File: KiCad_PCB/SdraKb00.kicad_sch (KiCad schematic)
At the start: 20 parts, among them J1 USB_C_Receptacle_USB2.0_16P, SW1 Reset_SW, U1 ATMEGA32U4-AU, Y1 16MHz

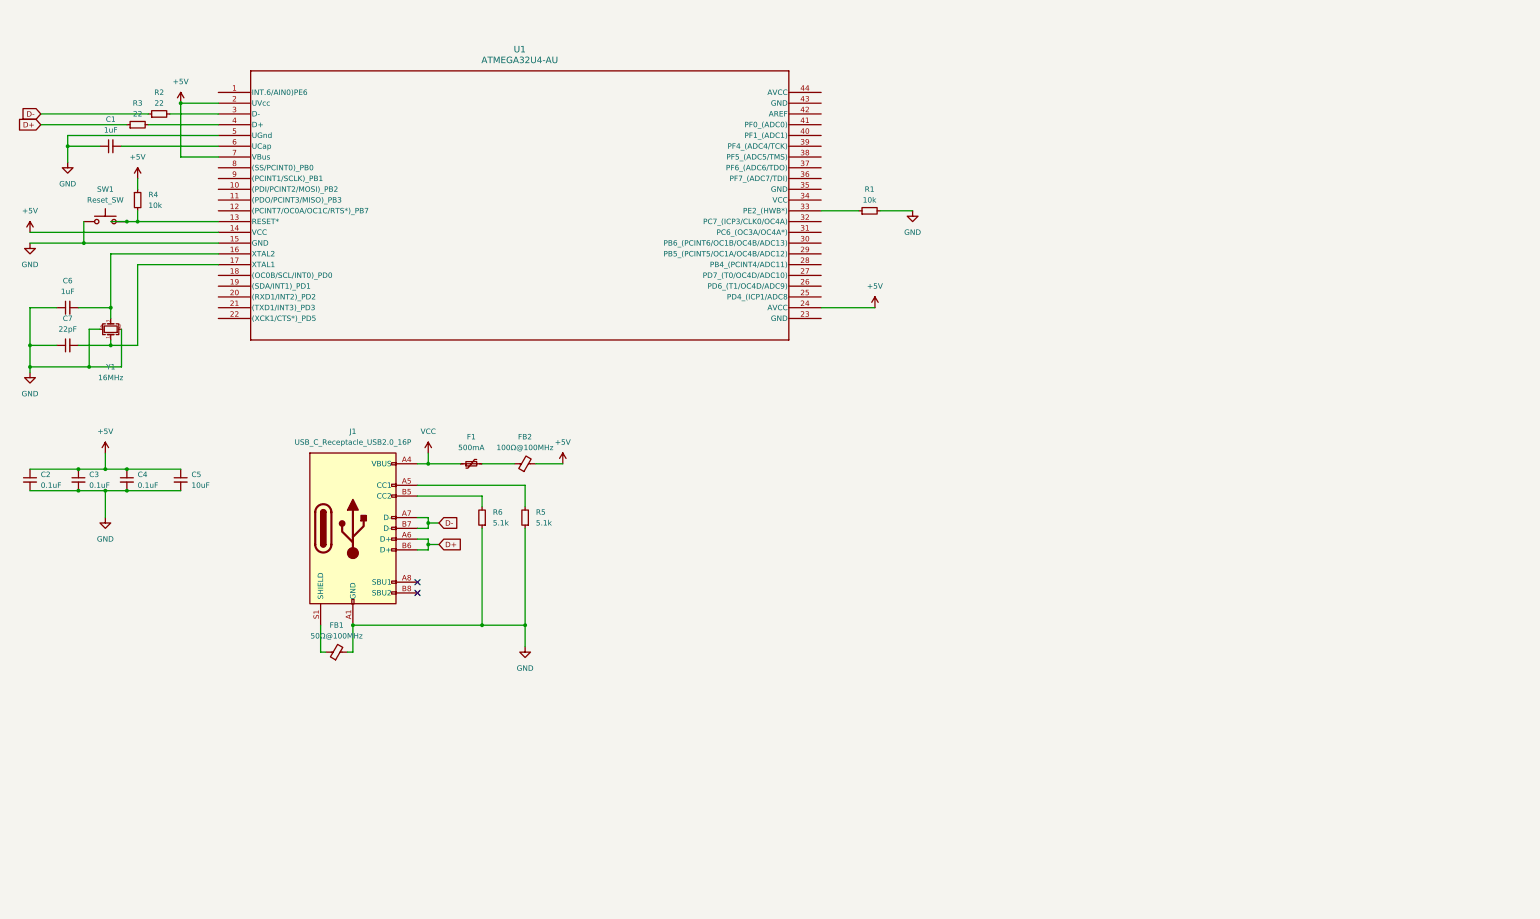
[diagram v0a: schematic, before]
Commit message: Adjusted first sketch based on masterzen.
https://www.masterzen.fr/2020/05/03/designing-a-keyboard-part-1/
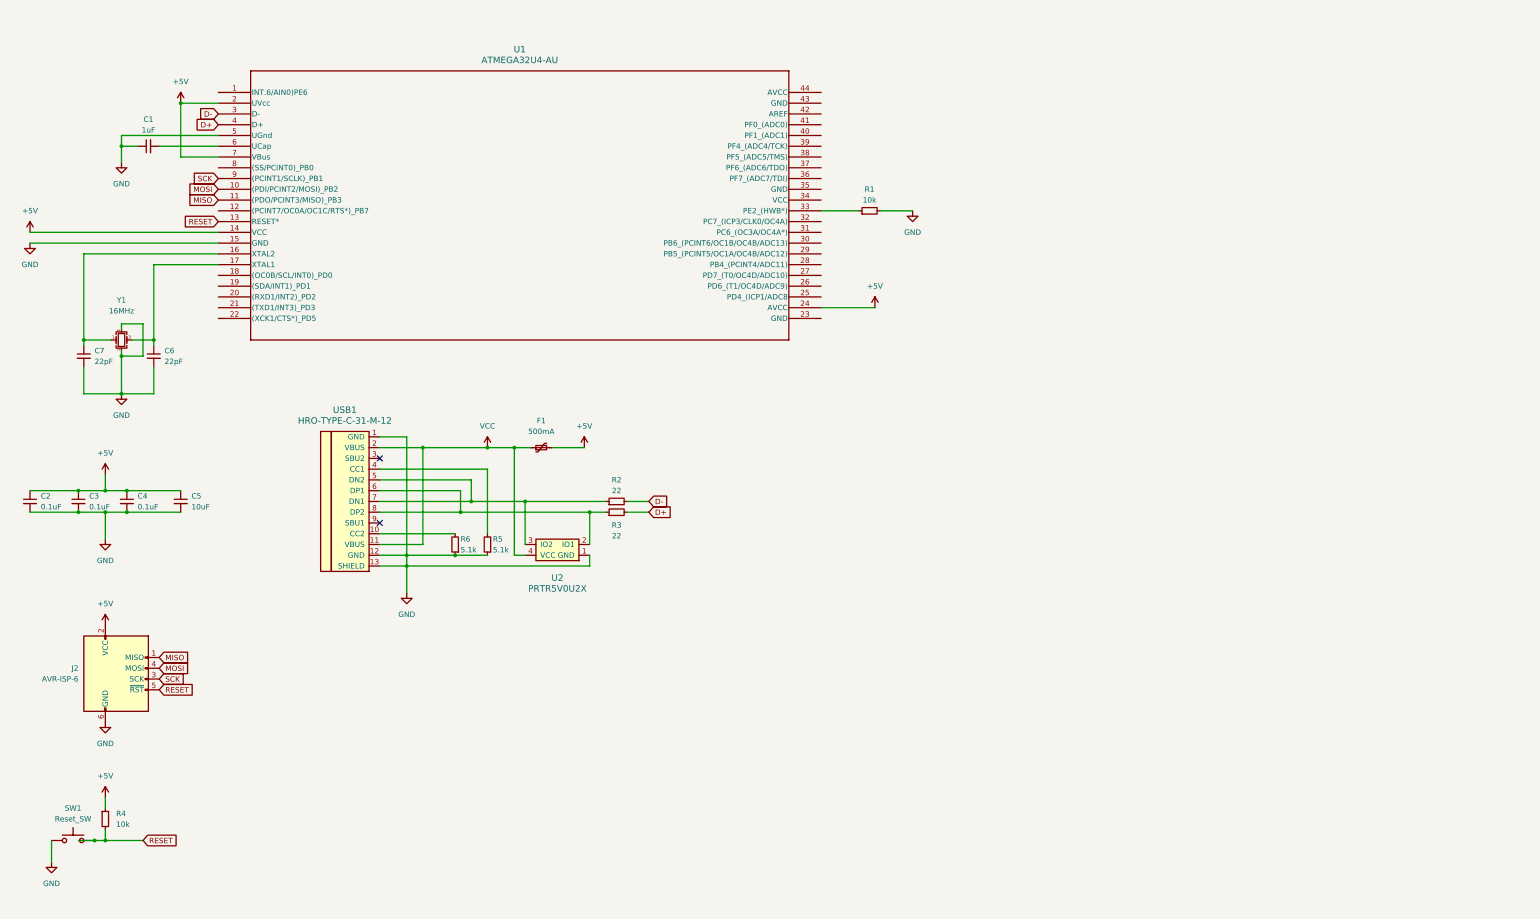
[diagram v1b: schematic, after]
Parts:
- removed FB1: 50Ω@100MHz, symbol Device:FerriteBead_Small
- removed FB2: 100Ω@100MHz, symbol Device:FerriteBead_Small
- removed J1: USB_C_Receptacle_USB2.0_16P, Connector_USB:USB_C_Receptacle_HRO_TYPE-C-31-M-12, symbol Connector:USB_C_Receptacle_USB2.0_16P
- added J2: AVR-ISP-6, symbol Connector:AVR-ISP-6
- added U2: PRTR5V0U2X, symbol random-keyboard-parts:PRTR5V0U2X
- added USB1: HRO-TYPE-C-31-M-12, symbol Type-C:HRO-TYPE-C-31-M-12
- C6: value 1uF -> 22pF
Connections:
- net +5V: now also F1.2, J2.2 (VCC)
- net D+: now also R3.2, U1.4 (D+); no longer R3.1
- net D-: now also R2.2, U1.3 (D-); no longer R2.1
- net GND: now also C6.2, C7.2, J2.6 (GND), U2.1 (GND), USB1.1 (GND), USB1.12 (GND), USB1.13 (SHIELD); no longer C6.1, C7.1
- net VCC: now also U2.4 (VCC), USB1.11 (VBUS), USB1.2 (VBUS)
- net RESET: now reaches R4.2, SW1.2, U1.13 (RESET*)
- net RESET: now also J2.5 (~{RST})
- net at R6.2: now also USB1.10 (CC2)
- net MOSI: now reaches U1.10 ((PDI/PCINT2/MOSI)_PB2)
- net MOSI: now also J2.4 (MOSI)
- net MISO: now reaches U1.11 ((PDO/PCINT3/MISO)_PB3)
- net MISO: now also J2.1 (MISO)
- net SCK: now reaches U1.9 ((PCINT1/SCLK)_PB1)
- net SCK: now also J2.3 (SCK)
- net at R5.2: now also USB1.4 (CC1)
- new net: R3.1, U2.2 (IO1), USB1.6 (DP1), USB1.8 (DP2)
- new net: R2.1, U2.3 (IO2), USB1.5 (DN2), USB1.7 (DN1)
- new net: C7.1, U1.16 (XTAL2), Y1.1
- new net: C6.1, U1.17 (XTAL1), Y1.3
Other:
- moved on the sheet: C1, C2, C3, C4, C5, C6, C7, F1, R2, R3, R4, R5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

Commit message: Replaced AtMega32U4 with default library. Adding switch array.
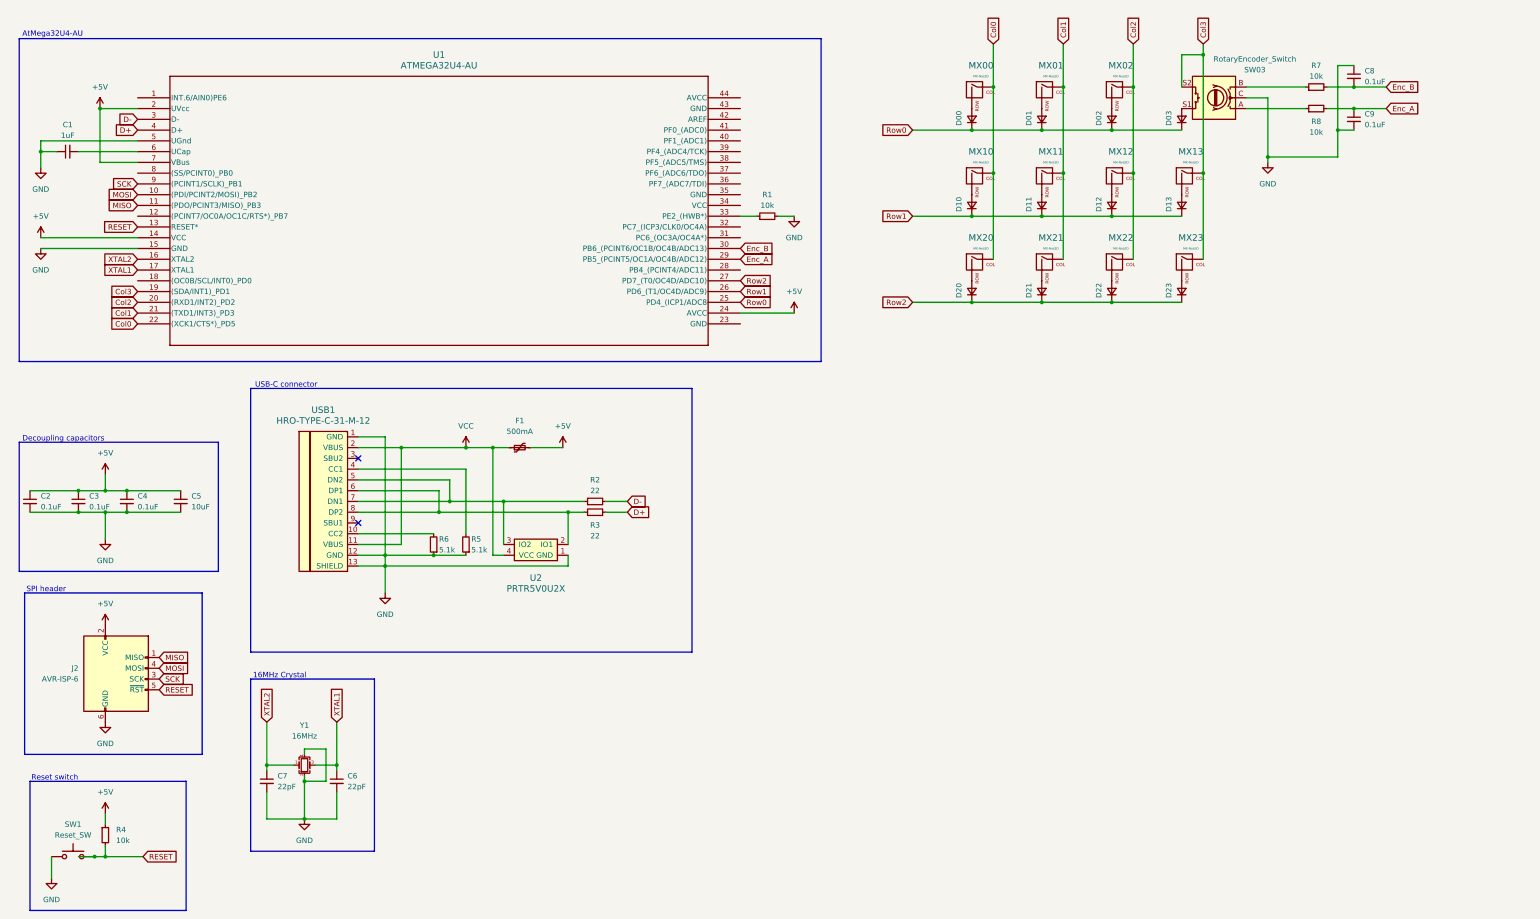
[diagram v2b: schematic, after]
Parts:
- added C8, C9: 0.1uF, symbol Device:C_Small
- added D00, D01, D02, D03, D10, D11, D12, D13, D20, D21, D22, D23: D_Small, symbol Device:D_Small
- added MX00, MX01, MX02, MX10, MX11, MX12, MX13, MX20, MX21, MX22, MX23: MX-NoLED, symbol MX_Alps_Hybrid:MX-NoLED
- added R7, R8: 10k, symbol Device:R_Small
- added SW03: RotaryEncoder_Switch, symbol Device:RotaryEncoder_Switch
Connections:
- net GND: now also C8.1, C9.2, SW03.C
- net XTAL2: now reaches C7.1, U1.16 (XTAL2), Y1.1
- net XTAL1: now reaches C6.1, U1.17 (XTAL1), Y1.3
- net Col3: now reaches U1.19 ((SDA/INT1)_PD1)
- net Col3: now also MX13.1 (COL), MX23.1 (COL), SW03.S2
- net Col2: now reaches U1.20 ((RXD1/INT2)_PD2)
- net Col2: now also MX02.1 (COL), MX12.1 (COL), MX22.1 (COL)
- net Col1: now reaches U1.21 ((TXD1/INT3)_PD3)
- net Col1: now also MX01.1 (COL), MX11.1 (COL), MX21.1 (COL)
- net Col0: now reaches U1.22 ((XCK1/CTS*)_PD5)
- net Col0: now also MX00.1 (COL), MX10.1 (COL), MX20.1 (COL)
- net Row0: now reaches U1.25 (PD4_(ICP1/ADC8)
- net Row0: now also D00.1 (K), D01.1 (K), D02.1 (K), D03.1 (K)
- net Row1: now reaches U1.26 (PD6_(T1/OC4D/ADC9))
- net Row1: now also D10.1 (K), D11.1 (K), D12.1 (K), D13.1 (K)
- net Row2: now reaches U1.27 (PD7_(T0/OC4D/ADC10))
- net Row2: now also D20.1 (K), D21.1 (K), D22.1 (K), D23.1 (K)
- net Enc_A: now reaches U1.29 (PB5_(PCINT5/OC1A/OC4B/ADC12))
- net Enc_A: now also C9.1, R8.2
- net Enc_B: now reaches U1.30 (PB6_(PCINT6/OC1B/OC4B/ADC13))
- net Enc_B: now also C8.2, R7.2
- new net: R8.1, SW03.A
- new net: R7.1, SW03.B
- new net: D03.2 (A), SW03.S1
- new net: D11.2 (A), MX11.2 (ROW)
- new net: D01.2 (A), MX01.2 (ROW)
- new net: D21.2 (A), MX21.2 (ROW)
- new net: D23.2 (A), MX23.2 (ROW)
- new net: D00.2 (A), MX00.2 (ROW)
- new net: D20.2 (A), MX20.2 (ROW)
- new net: D12.2 (A), MX12.2 (ROW)
- new net: D10.2 (A), MX10.2 (ROW)
- new net: D22.2 (A), MX22.2 (ROW)
- new net: D13.2 (A), MX13.2 (ROW)
- new net: D02.2 (A), MX02.2 (ROW)
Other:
- note added: "16MHz Crystal"
- note added: "AtMega32U4-AU"
- note added: "Decoupling capacitors"
- note added: "Reset switch"
- note added: "SPI header"
- note added: "USB-C connector"
- moved on the sheet: C1, C6, C7, F1, R1, R2, R3, R4, R5, R6, SW1, U1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

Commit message: Adding RGB chain.
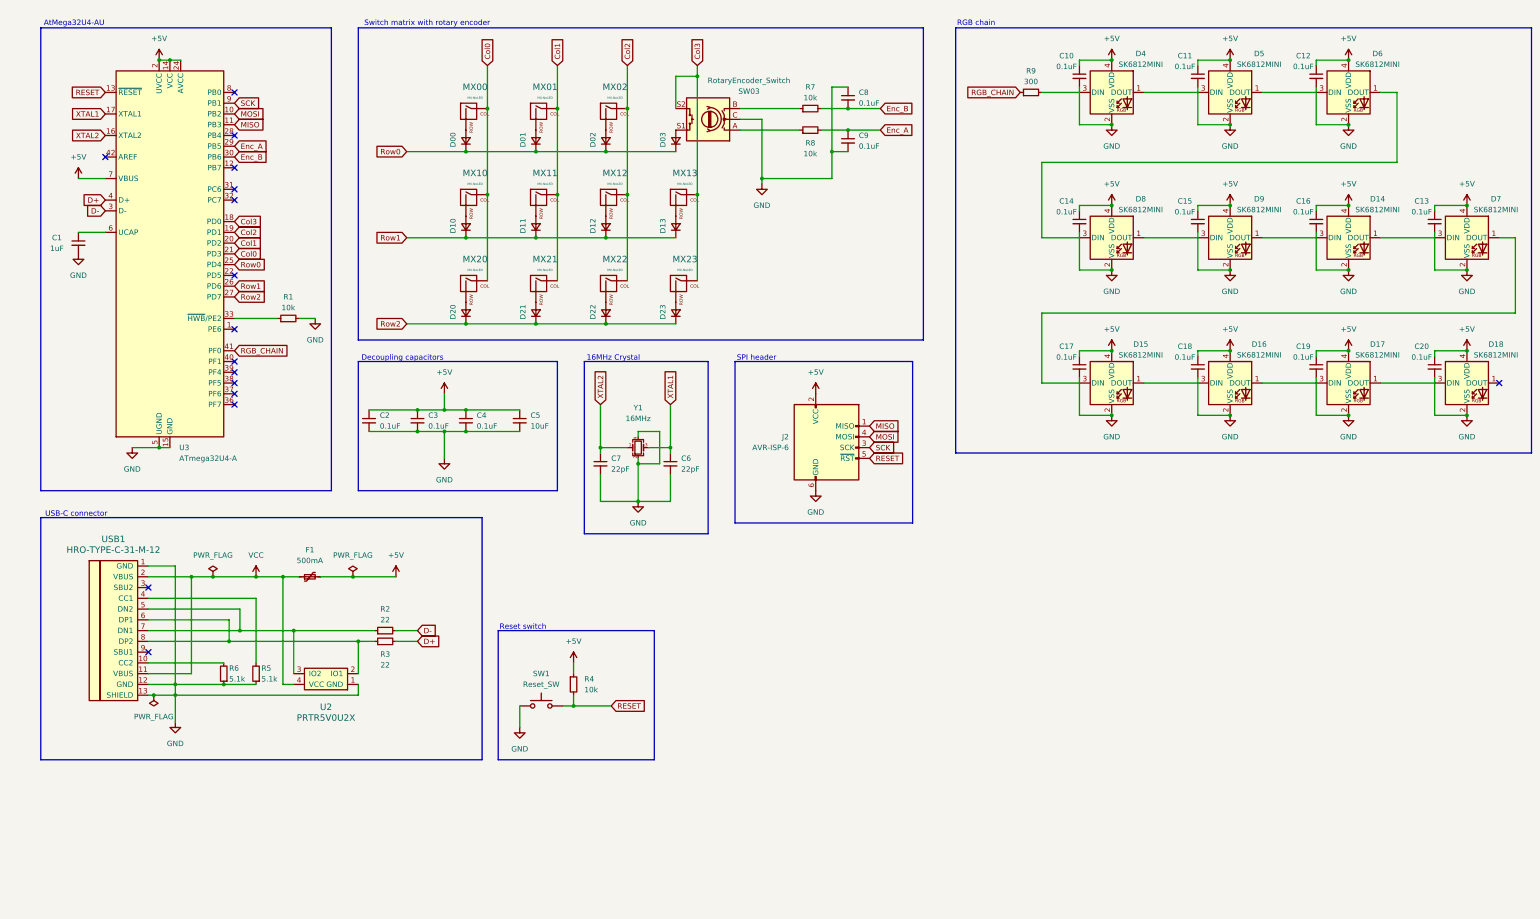
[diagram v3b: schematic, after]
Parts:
- removed U1: ATMEGA32U4-AU, atmega32u4-au:44ML_ATM-M, symbol atmega32u4-au:ATMEGA32U4-AU
- added C10, C11, C12, C13, C14, C15, C16, C17, C18, C19, C20: 0.1uF, symbol Device:C_Small
- added D14, D15, D16, D17, D18, D4, D5, D6, D7, D8, D9: SK6812MINI, LED_SMD:LED_SK6812MINI_PLCC4_3.5x3.5mm_P1.75mm, symbol LED:SK6812MINI
- added R9: 300, symbol Device:R_Small
- added U3: ATmega32U4-A, Package_QFP:TQFP-44_10x10mm_P0.8mm, symbol MCU_Microchip_ATmega:ATmega32U4-A
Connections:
- net +5V: now also C10.1, C11.1, C12.1, C13.1, C14.1, C15.1, C16.1, C17.1, C18.1, C19.1, C20.1, D14.4 (VDD), D15.4 (VDD), D16.4 (VDD), D17.4 (VDD), D18.4 (VDD), D4.4 (VDD), D5.4 (VDD), D6.4 (VDD), D7.4 (VDD), D8.4 (VDD), D9.4 (VDD), U3.14 (VCC), U3.2 (UVCC), U3.24 (AVCC), U3.34 (VCC), U3.44 (AVCC), U3.7 (VBUS)
- net Col0: now also U3.21 (PD3)
- net Col1: now also U3.20 (PD2)
- net Col2: now also U3.19 (PD1)
- net Col3: now also U3.18 (PD0)
- net D+: now also U3.4 (D+)
- net D-: now also U3.3 (D-)
- net Enc_A: now also U3.29 (PB5)
- net Enc_B: now also U3.30 (PB6)
- net GND: now also C1.2, C10.2, C11.2, C12.2, C13.2, C14.2, C15.2, C16.2, C17.2, C18.2, C19.2, C20.2, D14.2 (VSS), D15.2 (VSS), D16.2 (VSS), D17.2 (VSS), D18.2 (VSS), D4.2 (VSS), D5.2 (VSS), D6.2 (VSS), D7.2 (VSS), D8.2 (VSS), D9.2 (VSS), U3.15 (GND), U3.23 (GND), U3.35 (GND), U3.43 (GND), U3.5 (UGND); no longer C1.1
- net MISO: now also U3.11 (PB3)
- net MOSI: now also U3.10 (PB2)
- net RESET: now also U3.13 (~{RESET})
- net Row0: now also U3.25 (PD4)
- net Row1: now also U3.26 (PD6)
- net Row2: now also U3.27 (PD7)
- net SCK: now also U3.9 (PB1)
- net XTAL1: now also U3.17 (XTAL1)
- net XTAL2: now also U3.16 (XTAL2)
- net at R1.1: now also U3.33 (~{HWB}/PE2)
- new net: D17.1 (DOUT), D18.3 (DIN)
- new net: D16.1 (DOUT), D17.3 (DIN)
- new net: D6.1 (DOUT), D8.3 (DIN)
- new net: D5.1 (DOUT), D6.3 (DIN)
- new net: D15.3 (DIN), D7.1 (DOUT)
- new net: D14.1 (DOUT), D7.3 (DIN)
- new net: D14.3 (DIN), D9.1 (DOUT)
- new net: D4.1 (DOUT), D5.3 (DIN)
- new net: D8.1 (DOUT), D9.3 (DIN)
- new net: D15.1 (DOUT), D16.3 (DIN)
- new net: C1.1, U3.6 (UCAP)
- new net: D4.3 (DIN), R9.2
- new net RGB_CHAIN: R9.1, U3.41 (PF0)
- no-connect marks 2 -> 16
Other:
- note added: "RGB chain"
- note added: "Switch matrix with rotary encoder"
- moved on the sheet: C2, C3, C4, C5, C6, C7, C8, C9, D00, D01, D02, D03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

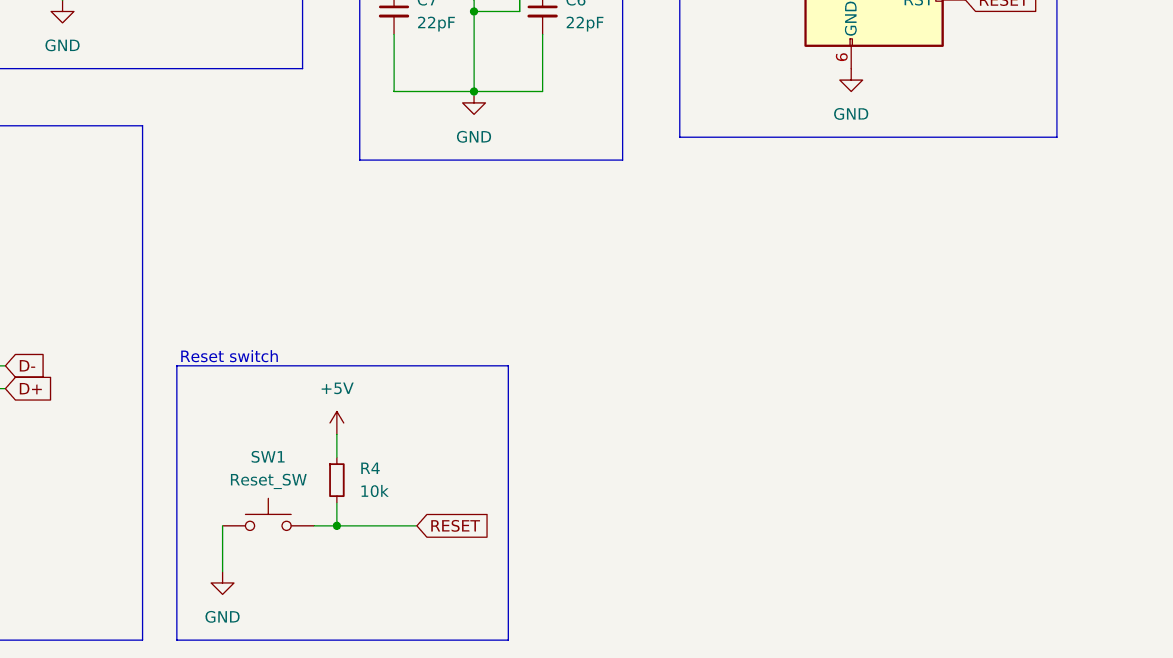
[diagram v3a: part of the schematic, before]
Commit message: Adding mounting holes.
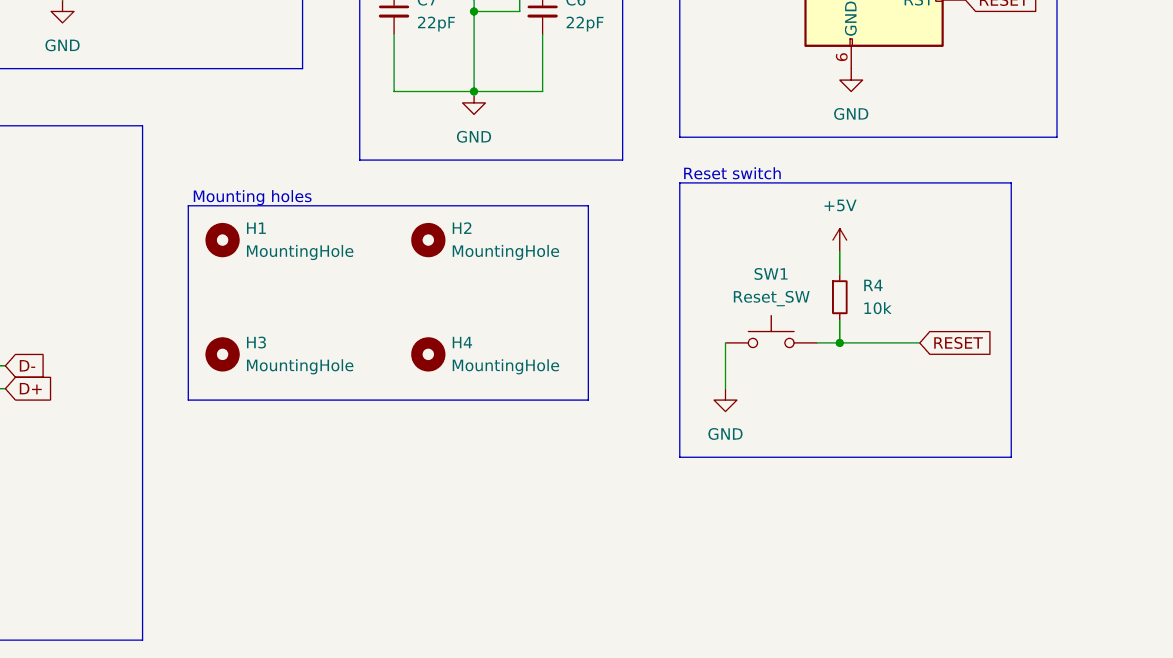
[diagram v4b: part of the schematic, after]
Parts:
- added H1, H2, H3, H4: MountingHole, symbol Mechanical:MountingHole
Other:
- note added: "Mounting holes"
- moved on the sheet: R4, SW1
